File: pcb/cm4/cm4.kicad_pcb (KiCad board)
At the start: 4 copper layers, 100 x 80 mm, 32 parts, among them J101 Conn_02x10_Row_Letter_First, J201 DF40C-100DS-0.4V_51_, J202 DF40C-100DS-0.4V_51_, J301 HR911130A, U201 SN74LV1T34DBV, U301 TPD4EUSB30, U302 TPD4EUSB30, U401 RT9742GGJ5

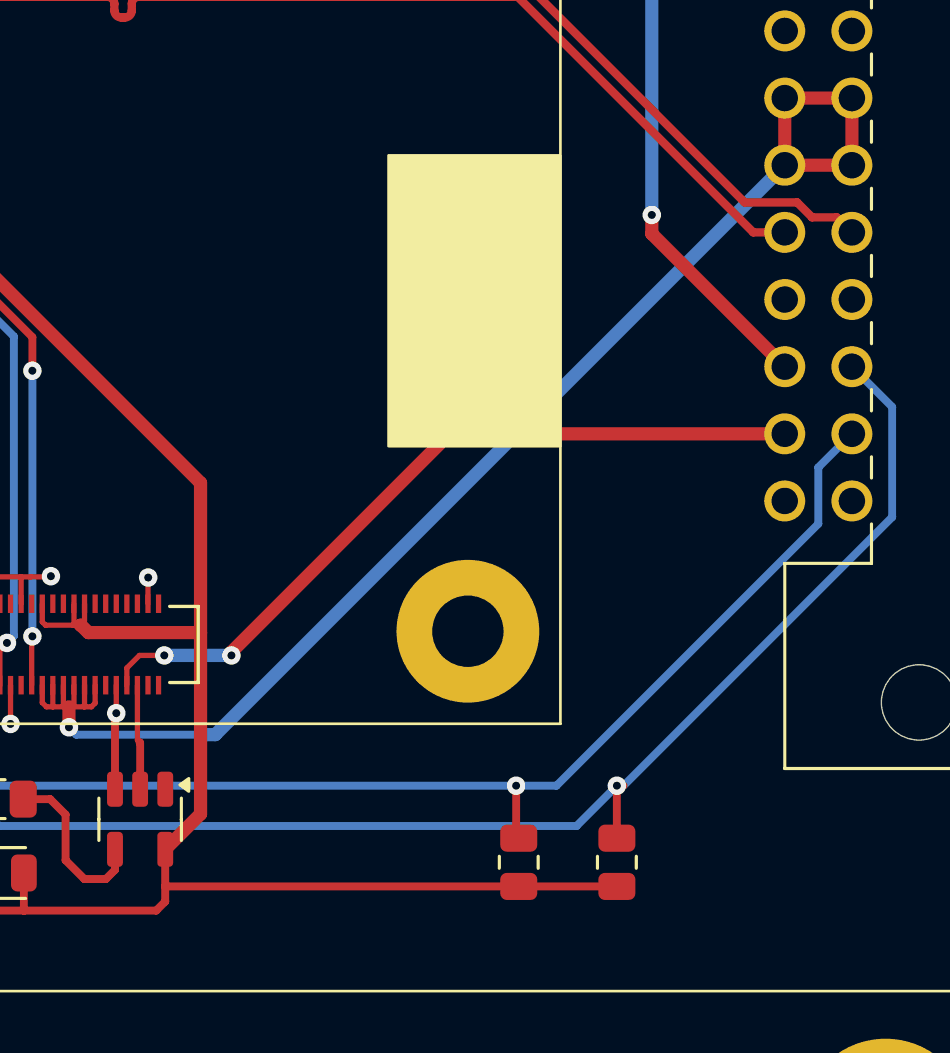
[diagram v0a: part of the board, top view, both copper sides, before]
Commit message: add more caps
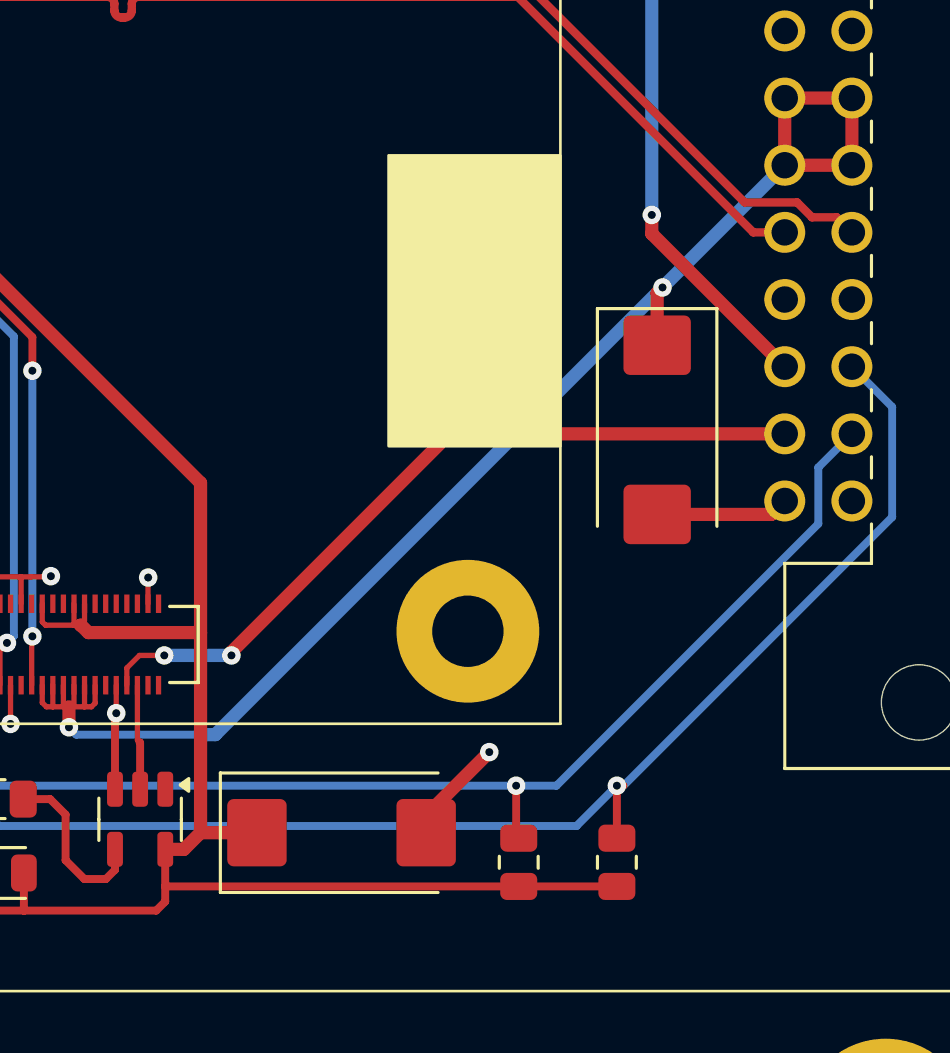
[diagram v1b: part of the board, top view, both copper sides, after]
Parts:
- added C101: 100u / 25V, Capacitor_Tantalum_SMD:CP_EIA-7343-43_Kemet-X_Pad2.25x2.55mm_HandSolder, F.Cu at (179.6, 94.6)
- added C201: 100u / 25V, Capacitor_Tantalum_SMD:CP_EIA-7343-43_Kemet-X_Pad2.25x2.55mm_HandSolder, F.Cu at (167.6, 109.8)
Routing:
- net GND: track 106.5 -> 115.9 mm, vias 43 -> 44
- net +3V3: track 167.6 -> 170.2 mm
- net +5V: track 53.8 -> 56.1 mm, vias 1 -> 2

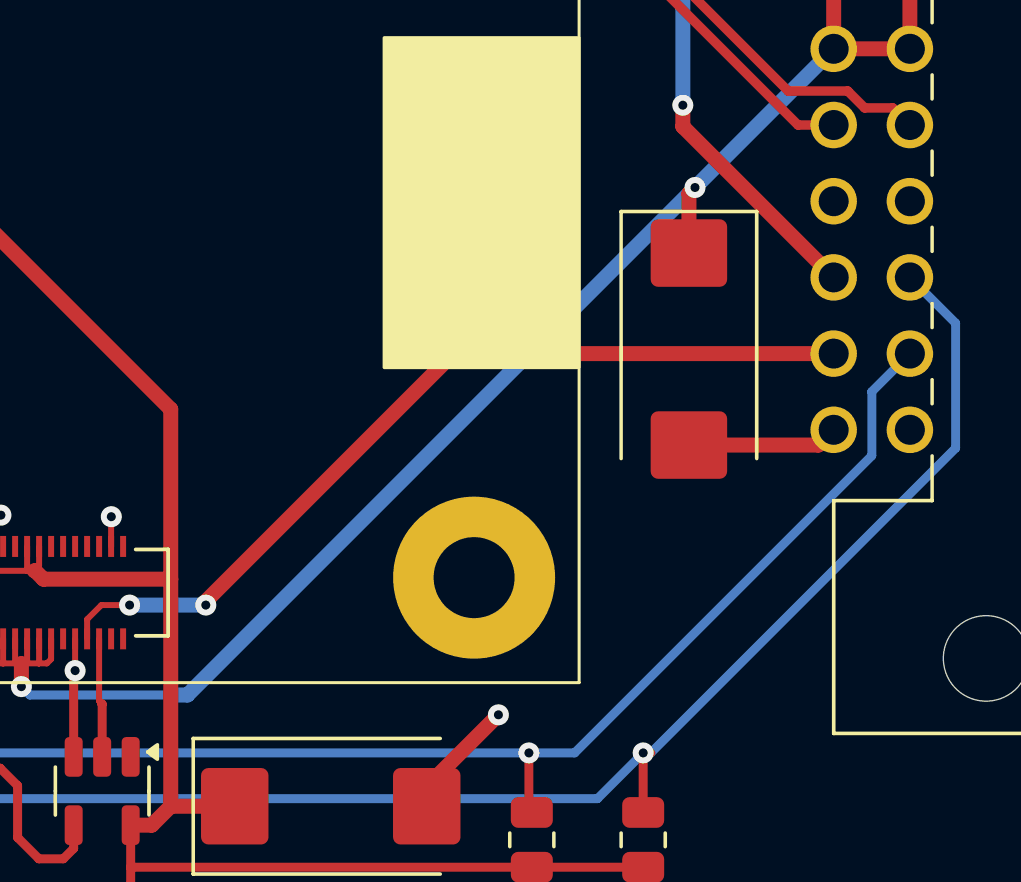
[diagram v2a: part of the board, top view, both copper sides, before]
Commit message: re-rout some routes
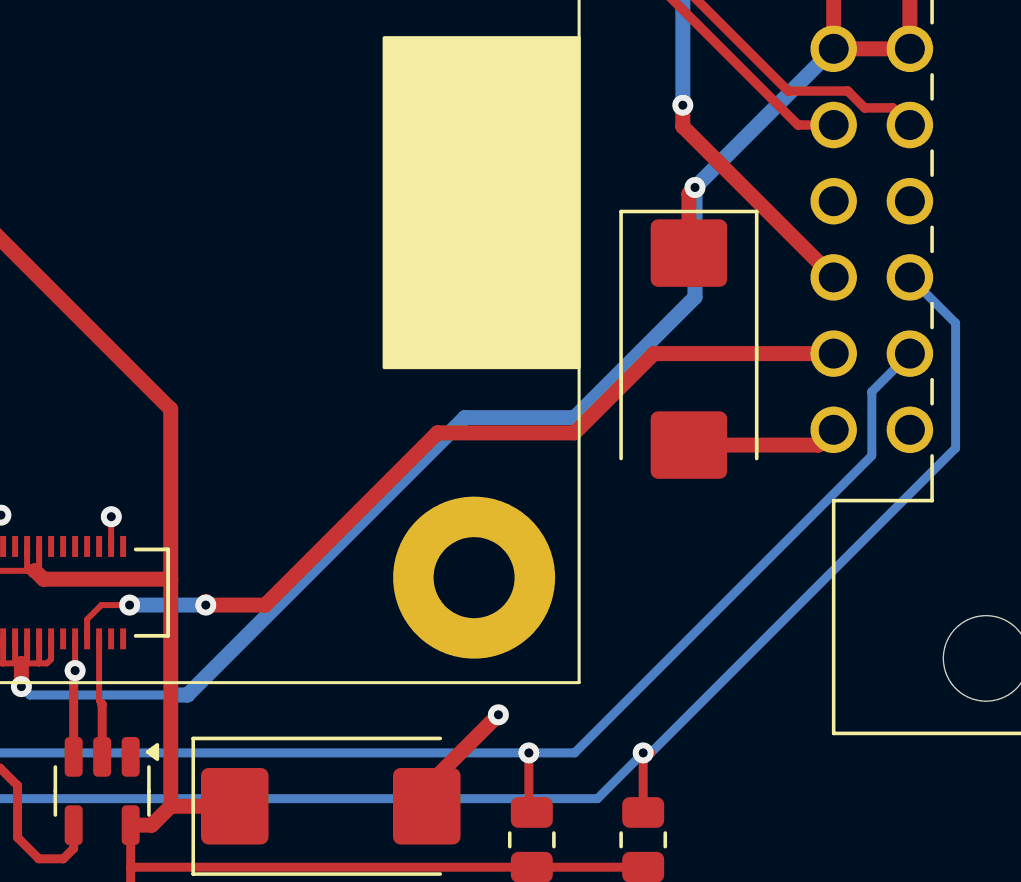
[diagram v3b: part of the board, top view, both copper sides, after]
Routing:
- net +5V: track 56.1 -> 58.2 mm
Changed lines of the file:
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@@
 	)
 	(segment
-		(start 171.7338 94.714)
+		(start 165.4596 103.0964)
+		(end 171.2 97.356)
+		(width 0.5)
+		(layer "F.Cu")
+		(net 9)
+	)
+	(segment
+		(start 178.414 94.714)
 		(end 184.408 94.714)
+		(width 0.5)
+		(layer "F.Cu")
+		(net 9)
+	)
+	(segment
+		(start 175.772 97.356)
+		(end 178.414 94.714)
+		(width 0.5)
+		(layer "F.Cu")
+		(net 9)
+	)
+	(segment
+		(start 163.4784 103.0964)
+		(end 165.4596 103.0964)
 		(width 0.5)
 		(layer "F.Cu")
@@
 	)
 	(segment
-		(start 163.4784 102.9694)
-		(end 171.7338 94.714)
+		(start 171.2 97.356)
+		(end 175.772 97.356)
 		(width 0.5)
 		(layer "F.Cu")
@@
 	)
 	(segment
-		(start 179.785 89.177)
-		(end 162.8684 106.0936)
+		(start 179.785 92.835)
+		(end 179.785 89.177)
+		(width 0.5)
+		(layer "B.Cu")
+		(net 13)
+	)
+	(segment
+		(start 162.8684 106.0936)
+		(end 172.114 96.848)
+		(width 0.5)
+		(layer "B.Cu")
+		(net 13)
+	)
+	(segment
+		(start 175.772 96.848)
+		(end 179.785 92.835)
 		(width 0.5)
 		(layer "B.Cu")
@@
 		(width 0.5)
 		(layer "B.Cu")
+		(net 13)
+	)
+	(segment
+		(start 172.114 96.848)
+		(end 175.772 96.848)
+		(width 0.5)
+		(layer "B.Cu")

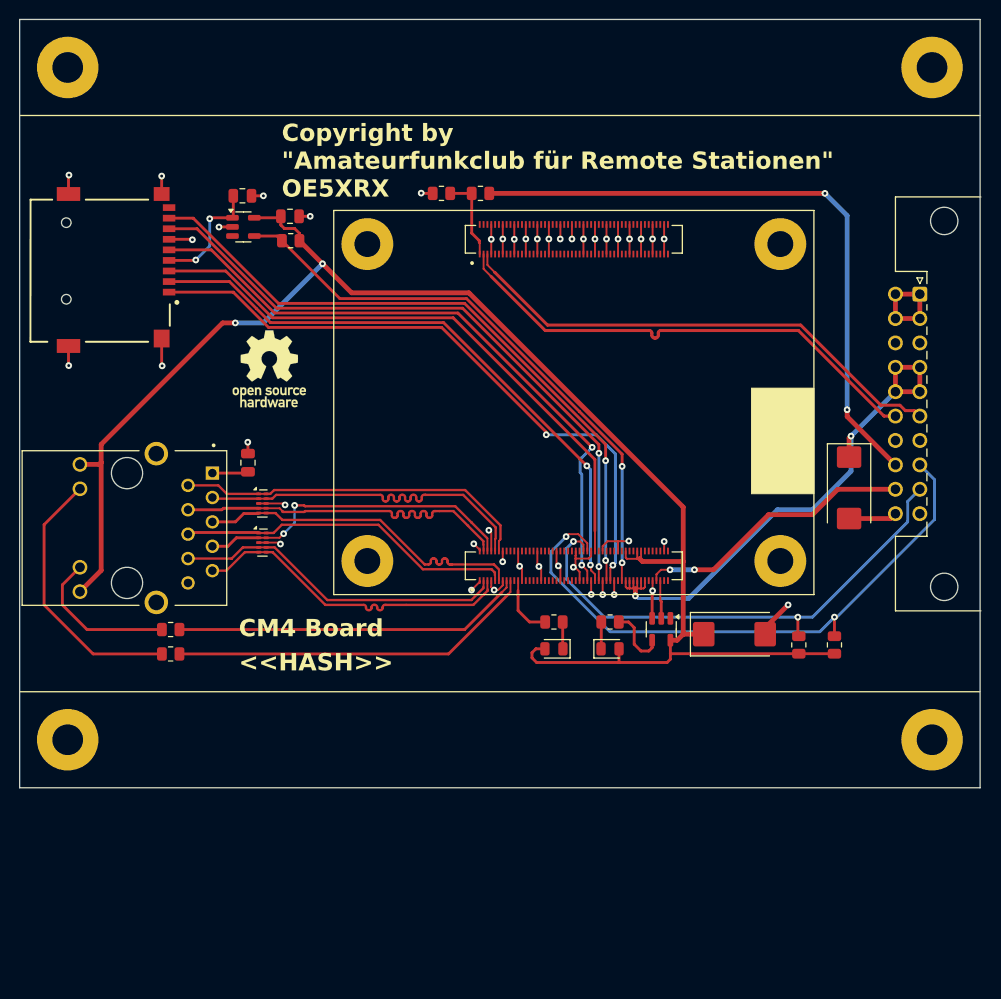
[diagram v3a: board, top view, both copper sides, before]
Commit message: update pcb size
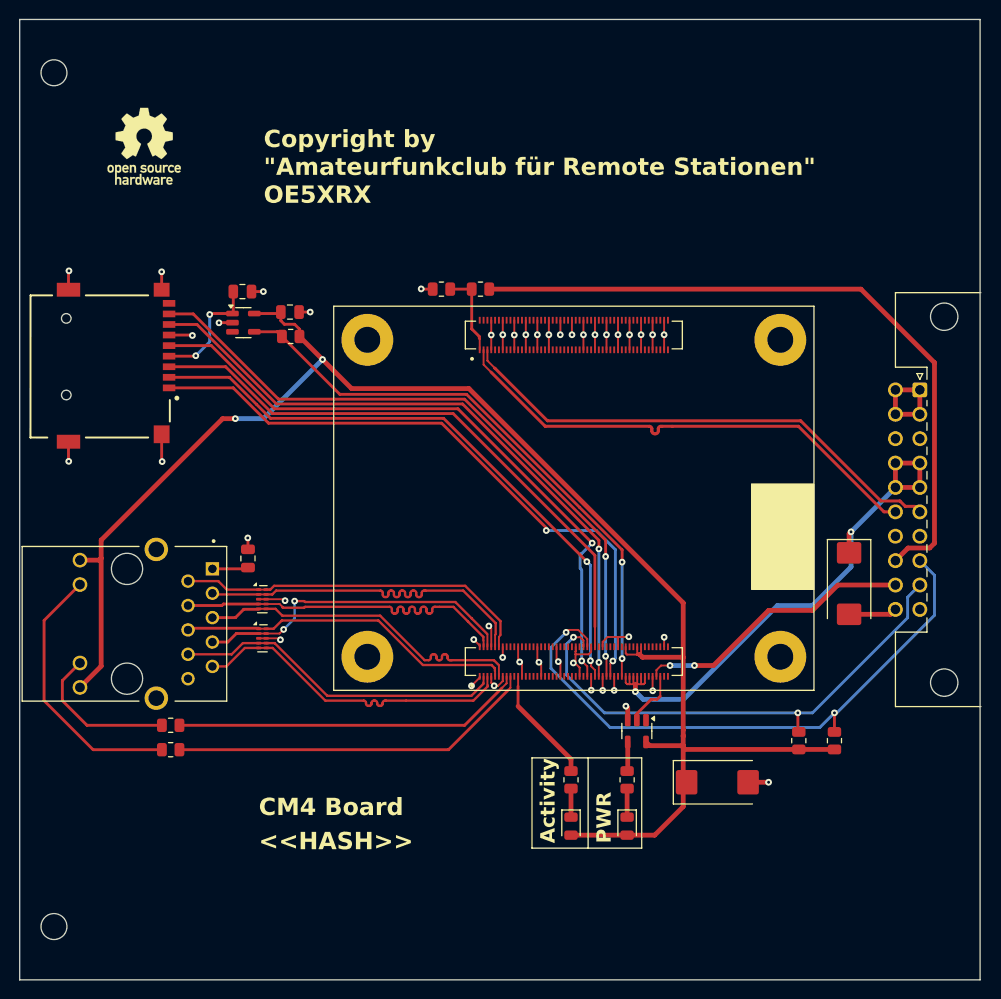
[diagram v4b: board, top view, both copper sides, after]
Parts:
- removed the REF** at (188.2, 50.8)
- removed the REF** at (98.2, 50.8)
- removed the REF** at (188.2, 120.8)
- removed the REF** at (98.2, 120.8)
- added H101: MountingHole, MountingHole:MountingHole_2.7mm_M2.5, F.Cu at (96.8, 51.3)
- added H102: MountingHole, MountingHole:MountingHole_2.7mm_M2.5, F.Cu at (96.8, 140.2)
- moved #SYM101 26.6 mm to (106.2, 59.0)
- moved D201 18.6 mm to (150.6, 129.8), turned to -90 degrees
- moved D202 18.6 mm to (156.5, 129.8), turned to -90 degrees
- moved R201 16.5 mm to (150.6, 125.0), turned to 90 degrees
- moved R204 16.5 mm to (156.5, 125.0), turned to 90 degrees
- moved C201 15.5 mm to (165.9, 125.2)
- moved U201 10.9 mm to (157.5, 119.9)
- moved C402 9.97 mm to (116.4, 74.1)
- moved R301 9.97 mm to (108.9, 121.8)
- moved U302 9.97 mm to (118.5, 106.2)
- moved C101 9.97 mm to (179.6, 104.5)
- moved C301 9.97 mm to (117.0, 101.9)
- moved C401 9.97 mm to (121.4, 76.3)
- moved J101 9.97 mm to (186.9, 84.4)
- moved J201 9.97 mm to (150.9, 112.7)
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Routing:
- net /USB_OTG_ID: track 66.3 -> 73.1 mm, vias 2 -> 0
- net /CM4-Board/LED_nACTIVITY: track 6.44 -> 12.1 mm
- net Net-(U201-Y): track 6.66 -> 3.06 mm
- net GND: track 115.9 -> 112.8 mm, vias 44 -> 45
- net /CM4-Board/LED_nPWR: track 3.98 -> 5.93 mm
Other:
- board size 100 x 80 mm -> 100 x 100 mm
- board text added: "Activity"
- board text added: "PWR"

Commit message: fixes
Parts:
- H101, H102: footprint MountingHole:MountingHole_2.7mm_M2.5 -> MountingHole:MountingHole_3.2mm_M3
- moved H101 2.42 mm to (98.2, 53.3)
- moved H102 2.42 mm to (98.2, 138.3)
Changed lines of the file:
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@@
 		(allow_soldermask_bridges_in_footprints no)
 		(tenting front back)
-		(grid_origin 93.222 145.794)
+		(grid_origin 93.222 45.794)
 		(pcbplotparams
 			(layerselection 0x00000000_00000000_55555555_5755f5ff)
@@
 		)
 	)
-	(footprint "MountingHole:MountingHole_2.7mm_M2.5"
+	(footprint "MountingHole:MountingHole_3.2mm_M3"
 		(layer "F.Cu")
-		(at 96.792 140.244)
-		(descr "Mounting Hole 2.7mm, no annular, M2.5")
-		(tags "mounting hole 2.7mm no annular m2.5")
+		(at 98.222 138.294)
+		(descr "Mounting Hole 3.2mm, no annular, M3")
+		(tags "mounting hole 3.2mm no annular m3")
 		(property "Reference" "H102"
-			(at 0 -3.7 0)
+			(at 0 -4.2 0)
 			(layer "F.SilkS")
 			(hide yes)
@@
 		)
 		(property "Value" "MountingHole"
-			(at 0 3.7 0)
+			(at 0 4.2 0)
 			(layer "F.Fab")
 			(hide yes)
@@
 		(fp_circle
 			(center 0 0)
-			(end 2.7 0)
+			(end 3.2 0)
 			(stroke
 				(width 0.15)
@@
 		(fp_circle
 			(center 0 0)
-			(end 2.95 0)
+			(end 3.45 0)
 			(stroke
 				(width 0.05)
@@
 		(pad "" np_thru_hole circle
 			(at 0 0)
-			(size 2.7 2.7)
-			(drill 2.7)
+			(size 3.2 3.2)
+			(drill 3.2)
 			(layers "*.Cu" "*.Mask")
 		)
@@
 		)
 	)
-	(footprint "MountingHole:MountingHole_2.7mm_M2.5"
+	(footprint "MountingHole:MountingHole_3.2mm_M3"
 		(layer "F.Cu")
-		(at 96.792 51.344)
-		(descr "Mounting Hole 2.7mm, no annular, M2.5")
-		(tags "mounting hole 2.7mm no annular m2.5")
+		(at 98.222 53.294)
+		(descr "Mounting Hole 3.2mm, no annular, M3")
+		(tags "mounting hole 3.2mm no annular m3")
 		(property "Reference" "H101"
-			(at 0 -3.7 0)
+			(at 0 -4.2 0)
 			(layer "F.SilkS")
 			(hide yes)
@@
 		)
 		(property "Value" "MountingHole"
-			(at 0 3.7 0)
+			(at 0 4.2 0)
 			(layer "F.Fab")
 			(hide yes)
@@
 		(fp_circle
 			(center 0 0)
-			(end 2.7 0)
+			(end 3.2 0)
 			(stroke
 				(width 0.15)
@@
 		(fp_circle
 			(center 0 0)
-			(end 2.95 0)
+			(end 3.45 0)
 			(stroke
 				(width 0.05)
@@
 		(pad "" np_thru_hole circle
 			(at 0 0)
-			(size 2.7 2.7)
-			(drill 2.7)
+			(size 3.2 3.2)
+			(drill 3.2)
 			(layers "*.Cu" "*.Mask")
 		)
